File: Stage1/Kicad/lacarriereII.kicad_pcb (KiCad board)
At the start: 2 copper layers, 92 x 92 mm, 87 parts, among them J1 USB_C_Receptacle_USB2.0, J2 Conn_02x06, J3 Conn_01x06_Pin, U1 PCA9557PW, U10 XC6206P282MR, U11 XC6206P132MR, U12 ESP32_WROVER, U14 BME280, U16 BME280, U2 USBLC6-2SC6, U3 BQ25171QWDRCRQ1, U4 CH340C, U5 SIM800L-CORE, U6 UMH3N, U7 FS8205, U8 HY2112, U9 TLV61070A

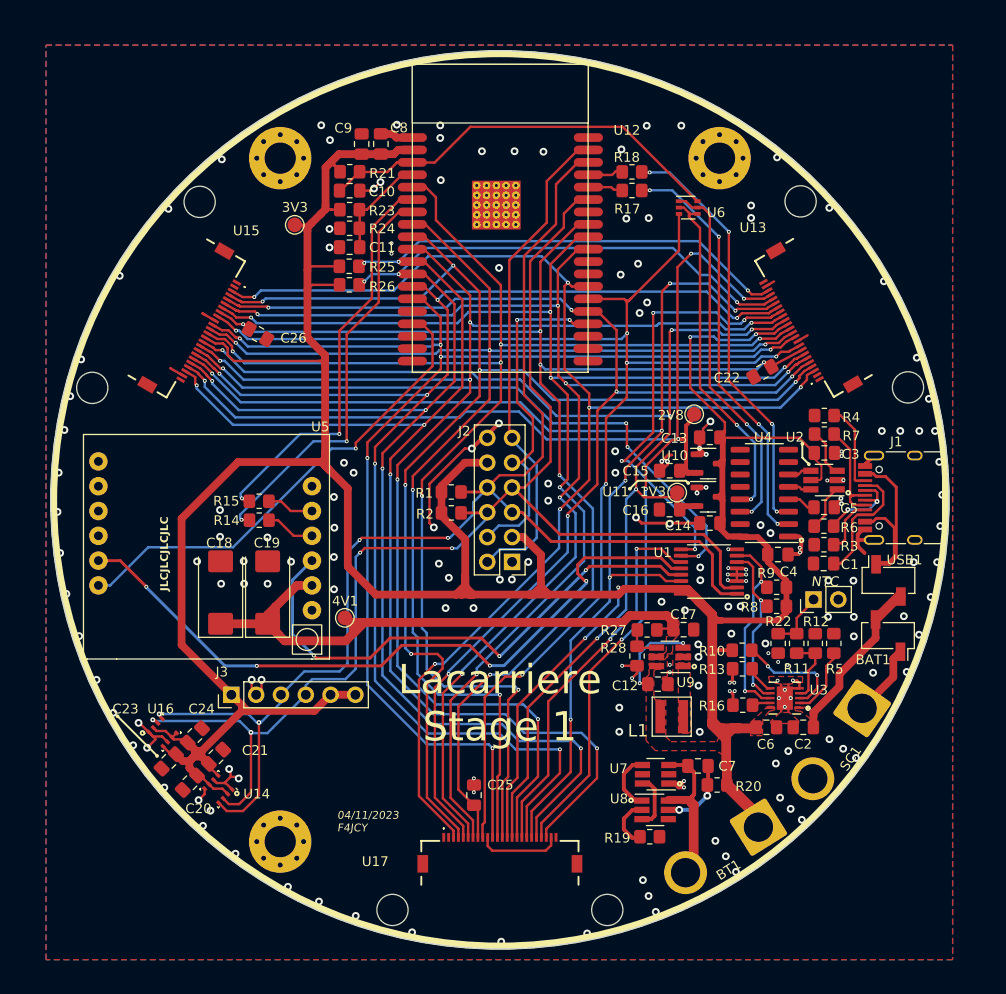
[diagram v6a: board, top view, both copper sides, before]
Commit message: [change] via size to be compatible witch jlc capabilities specs
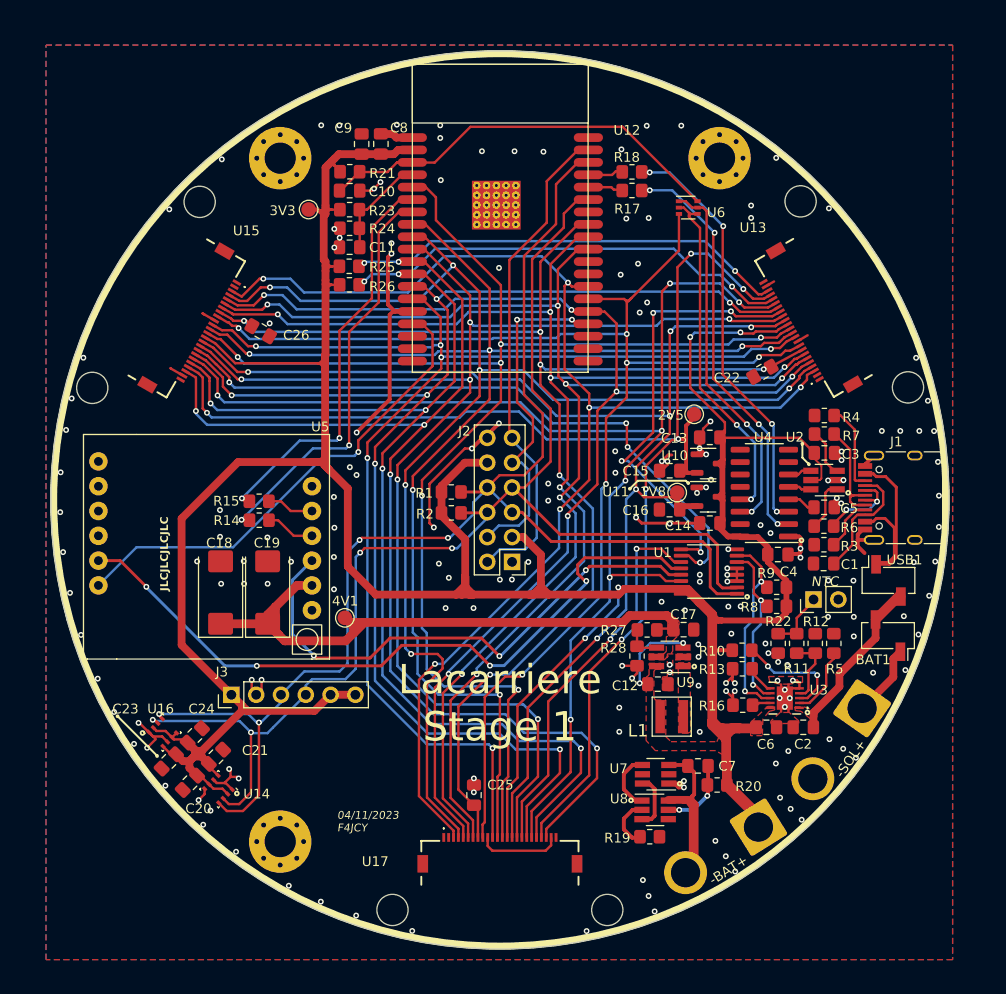
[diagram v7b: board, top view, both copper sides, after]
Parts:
- U10: value XC6206P282MR -> XC6206P252MR
- U11: value XC6206P132MR -> XC6206P182MR
- moved 3V3 2.12 mm to (80.4, 70.3)
- moved C26 0.41 mm to (75.5, 82.7)
- renumbered BT1 to -BAT+, SC1 to -SOL+, 1V3 to 1V8, 2V8 to 2V5
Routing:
- net GND: track 110.0 -> 135.2 mm, vias 186 -> 184
- net +2V8: track 139.6 -> 142.7 mm
- net +3.3V: track 385.9 -> 382.9 mm
- net /PWDN_C2: track 66.1 -> 67.8 mm
- net /DVP_SDA: track 157.3 -> 158.8 mm
- net /D3: track 123.8 -> 125.2 mm
- net /D2: track 131.8 -> 132.9 mm
- net /DVP_SCL: track 155.0 -> 156.1 mm
- net /D1: track 134.9 -> 136.0 mm
- net /PWDN_C1: track 44.6 -> 45.4 mm
- net /RESET_CAM: track 133.6 -> 134.3 mm
- net /D0: track 132.0 -> 132.6 mm
- net /IO_EXT2: track 36.0 -> 35.5 mm
